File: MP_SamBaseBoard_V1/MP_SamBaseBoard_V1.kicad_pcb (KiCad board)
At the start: 4 copper layers, 80 x 60 mm, 142 parts, among them J1 MOTOR-A_CONN, J10 P1_CONN, J11 I2C_CONN, J12 I2C_CONN, J13 SAM_SWD, J14 WS2812_EXT, J15 PWR_JACK, J16 USB_B_Micro, J17 BATT_CONN, J2 MOTOR-B_CONN, J3 Adafruit_Feather_CONN, J4 DM3D-SF, J5 Conn_01x02, J6 Conn_01x02, J7 SERVO_CONN, J8 P3_CONN, J9 P2_CONN, Q1 DMP3098L, SW1 RESET, SW2 3v3_PWR_SW, SW3 SW1, SW4 SW2, U1 ESP32-WROOM-32, U10 MPU-6050, U11 IRFHM9331PbF, U12 BD5291FVE-GTR, U13 SST25VF016B-50-4C-S2AF, U2 ATSAMD51J19A-A, U3 74LVC1G125, U4 TPS62135, U5 TPS62086, U6 MAX98357AETE, U7 DRV8833RTY, U8 HDC1080, U9 MCP73871-1CC, Y1 Crystal

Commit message: update
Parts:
- removed C32, C33: 4.7uF, Capacitor_SMD:C_0603_1608Metric
- removed C44: 0.1uF, Capacitor_SMD:C_0603_1608Metric
- removed D3: LED, LED_SMD:LED_0603_1608Metric
- removed D8: PWR_LED, LED_SMD:LED_0603_1608Metric
- removed G***: LOGO, GiraffeTech-Utility:MakerPlayground_BaseBoard_logo
- removed G***: LOGO, GiraffeTech-Utility:MakerPlayground_logo_4x4mm
- removed J6: Conn_01x02, GiraffeTech-Connector:DINKLE_EK500V-2P
- removed L2: 0.47uH, GiraffeTech-Inductor:L_0806_2016Metric
- removed R23, R26, R27, R28: 10K, Resistor_SMD:R_0603_1608Metric
- removed R29: 820K, Resistor_SMD:R_0603_1608Metric
- removed R39: 1K, Resistor_SMD:R_0603_1608Metric
- removed the REF** at (185.1, 130.1)
- removed U12: BD5291FVE-GTR, Package_TO_SOT_SMD:SOT-353_SC-70-5
- added H1: 3.5mm, MountingHole:MountingHole_3.5mm, F.Cu at (218.8, 93.5)
- added H2: 3.5mm, MountingHole:MountingHole_3.5mm, F.Cu at (218.8, 102.1)
- added H3: 3.5mm, MountingHole:MountingHole_3.5mm, F.Cu at (227.3, 93.5)
- added H4: 3.5mm, MountingHole:MountingHole_3.5mm, F.Cu at (227.3, 102.1)
- added Q2: ALS-PT19-315C/L177/TR8, Diode_SMD:D_0603_1608Metric, F.Cu at (233.6, 90.5)
- C14: value 10uF -> 0.1uF; footprint Capacitor_Tantalum_SMD:CP_EIA-3216-12_Kemet-S -> Capacitor_SMD:C_0603_1608Metric
- C21: value 0.1uF -> 4.7uF
- C23: value 10uF 16V -> 10uF
- C26: value 10uF -> 4.7uF; footprint Capacitor_Tantalum_SMD:CP_EIA-3216-12_Kemet-S -> Capacitor_SMD:C_0603_1608Metric
- C28, C29: value 0.1uF -> 10uF; footprint Capacitor_SMD:C_0603_1608Metric -> Capacitor_Tantalum_SMD:CP_EIA-3216-12_Kemet-S
- C30: value 2.2nF -> 0.1uF
- C31: value 1uF -> 0.1uF
- J1: value MOTOR-A_CONN -> MA_CONN; footprint GiraffeTech-Connector:DINKLE_EK500V-2P -> GiraffeTech-Connector:TerminalBlock_DEGSON_DG300-5-2pol
- J2: value MOTOR-B_CONN -> MB_CONN; footprint GiraffeTech-Connector:DINKLE_EK500V-2P -> GiraffeTech-Connector:TerminalBlock_DEGSON_DG300-5-2pol
- J4: value DM3D-SF -> LOAD_CONN; footprint Connector_Card:microSD_HC_Hirose_DM3D-SF -> GiraffeTech-Connector:TerminalBlock_DEGSON_DG300-5-3pol
- J5: value Conn_01x02 -> SPEAKER
- L3: footprint GiraffeTech-Inductor:L_1616_2020Metric -> GiraffeTech-Inductor:SPM6530T
- R11: value 10K -> 780
- R13, R17: value 10K -> 1K
- R14: value 10K -> 20K
- R16, R18, R20: value 1K -> 10K
- R19: value 2K -> 1K
- R2: value 1M -> 10K
- SW1, SW3, SW4: footprint Button_Switch_SMD:SW_SPST_B3S-1000 -> GiraffeTech-Electromechanical:SW_Push_TS-1145A-B-A
- SW2: footprint GiraffeTech-Electromechanical:SW_SPDT_CK-JS102011JCQN -> GiraffeTech-Alps:SSSS811101
- U10: value MPU-6050 -> KXTJ3-1057; footprint Sensor_Motion:InvenSense_QFN-24_4x4mm_P0.5mm -> Package_LGA:LGA-12_2x2mm_P0.5mm
- U5: value TPS62086 -> PAM8301; footprint GiraffeTech-Texas:Texas_VSON7 -> Package_TO_SOT_SMD:SOT-23-6
- U6: value MAX98357AETE -> BQ24075; footprint Package_DFN_QFN:TQFN-16-1EP_3x3mm_P0.5mm_EP1.23x1.23mm -> Package_DFN_QFN:VQFN-16-1EP_3x3mm_P0.5mm_EP1.6x1.6mm_ThermalVias
- U8: value HDC1080 -> Sensirion_SHT3x; footprint Package_SON:Texas_PWSON-N6 -> GiraffeTech-Sensiroin:Sensirion_SHT3x
- U9: value MCP73871-1CC -> LD39200PU33R; footprint Package_DFN_QFN:QFN-20-1EP_4x4mm_P0.5mm_EP2.5x2.5mm -> Package_DFN_QFN:DFN-6-1EP_3x3mm_P0.95mm_EP1.7x2.6mm
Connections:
- net Adf_D2 renamed ESP_RESET-D2
- net Adf_D3 renamed ESP_IO0-D3
- C14 pad 1: CHG_OUT -> Net-(C14-Pad1)
- C14 pad 2: GND -> Adf_A0_DAC0
- C17 pad 1: +3V3 -> +5V
- C18 pad 1: +5V -> VIN
- C21 pad 1: +3V3 -> CHG_OUT
- C23 pad 1: VIN -> CHG_OUT
- C28 pad 1: Net-(C28-Pad1) -> +3V3
- C29 pad 1: +3V3 -> +5V
- C30 pad 1: Net-(C30-Pad1) -> +3V3
- D1 pad 1: ~PG -> GND
- D2 pad 1: STAT1 -> GND
- J10 pad 3: Adf_A1_DAC1 -> D0_RxD0
- J10 pad 4: Adf_A0_DAC0 -> Adf_A1_DAC1
- J4 pad 1: Net-(J4-Pad1) -> VIN
- J4 pad 2: Adf_D13 -> Net-(J4-Pad2)
- J4 pad 3: SPI_MISO -> GND
- J8 pad 3: Adf_D4 -> Net-(J8-Pad3)
- J8 pad 4: Adf_A4 -> Adf_A3
- J9 pad 3: Adf_A3 -> D1_TxD0
- MK1 pad 1: Net-(C32-Pad2) -> Adf_A5
- R1 pad 2: Adf_D8 -> ESP_CS
- R11 pad 1: 3v3_EN -> ILIM
- R12 pad 1: +5V -> 3v3_EN
- R12 pad 2: CE -> GND
- R13 pad 1: +5V -> ISET
- R13 pad 2: ~TE -> GND
- R14 pad 1: +5V -> TMR
- R14 pad 2: PROG2 -> GND
- R15 pad 1: +5V -> TS
- R15 pad 2: REG_SEL -> GND
- R16 pad 1: +5V -> GND
- R16 pad 2: Net-(D1-Pad2) -> EN1
- R17 pad 1: PROG3 -> ~PGOOD
- R17 pad 2: GND -> Net-(D1-Pad2)
- R18 pad 1: +5V -> CHG_OUT
- R18 pad 2: Net-(D2-Pad2) -> EN2
- R19 pad 1: PROG1 -> ~CHG
- R19 pad 2: GND -> Net-(D2-Pad2)
- R2 pad 1: +3V3 -> Net-(R2-Pad1)
- R2 pad 2: Net-(R2-Pad2) -> +3V3
- R20 pad 1: +5V -> Adf_A4
- R20 pad 2: Net-(D3-Pad2) -> GND
- R21 pad 1: THERMAL -> +3V3
- R21 pad 2: GND -> I2C_SCL
- R22 pad 2: Net-(R22-Pad2) -> I2C_SDA
- SW3 pad 1: Adf_A1_DAC1 -> D0_RxD0
- SW4 pad 1: Adf_A3 -> D1_TxD0
- U1 pad 29: Adf_D8 -> ESP_CS-D8
- U1 pad 34: D0_RxD0 -> D1_TxD0
- U1 pad 35: D1_TxD0 -> D0_RxD0
- U1 pad 9: D0_RxD0 -> ESP_BUSY-D13
- U10 pad 10: Net-(C28-Pad1) -> +3V3
- U10 pad 11: GND -> +3V3
- U10 pad 12: Net-(U10-Pad12) -> I2C_SCL
- U10 pad 2: (no net) -> I2C_SDA
- U10 pad 3: (no net) -> +3V3
- U10 pad 4: (no net) -> GND
- U10 pad 5: (no net) -> Net-(U10-Pad5)
- U10 pad 6: Net-(U10-Pad6) -> GND
- U10 pad 7: Net-(U10-Pad7) -> +3V3
- U10 pad 8: +3V3 -> GND
- U10 pad 9: Net-(R22-Pad2) -> GND
- U11 pad 1: Net-(J6-Pad2) -> Net-(J4-Pad2)
- U11 pad 2: Net-(J6-Pad2) -> Net-(J4-Pad2)
- U11 pad 3: Net-(J6-Pad2) -> Net-(J4-Pad2)
- U2 pad 35: Adf_D13 -> ESP_BUSY-D13
- U2 pad 42: Adf_D8 -> ESP_CS-D8
- U5 pad 1: 3v3_EN -> Net-(J5-Pad2)
- U5 pad 2: Net-(R2-Pad2) -> GND
- U5 pad 3: +3V3 -> Net-(C14-Pad1)
- U5 pad 4: +3V3 -> Net-(R2-Pad1)
- U5 pad 5: GND -> +3V3
- U5 pad 6: Net-(L2-Pad1) -> Net-(J5-Pad1)
- U6 pad 1: Adf_D11 -> TS
- U6 pad 10: Net-(J5-Pad2) -> CHG_OUT
- U6 pad 11: GND -> CHG_OUT
- U6 pad 12: Net-(U6-Pad12) -> ILIM
- U6 pad 13: Net-(U6-Pad13) -> +5V
- U6 pad 14: Adf_D10 -> TMR
- U6 pad 16: D1_TxD0 -> ISET
- U6 pad 2: GND -> +BATT
- U6 pad 3: GND -> +BATT
- U6 pad 4: Net-(R23-Pad2) -> GND
- U6 pad 5: Net-(U6-Pad5) -> EN2
- U6 pad 6: Net-(U6-Pad6) -> EN1
- U6 pad 7: +3V3 -> ~PGOOD
- U6 pad 8: +3V3 -> GND
- U6 pad 9: Net-(J5-Pad1) -> ~CHG
- U8 pad 4: Net-(U8-Pad4) -> I2C_SCL
- U8 pad 6: I2C_SCL -> Net-(U8-Pad6)
- U8 pad 7: Net-(U8-Pad7) -> GND
- U9 pad 1: CHG_OUT -> +3V3
- U9 pad 2: +5V -> +3V3
- U9 pad 3: REG_SEL -> GND
- U9 pad 4: PROG2 -> Net-(U9-Pad4)
- U9 pad 5: THERMAL -> 3v3_EN
- U9 pad 6: ~PG -> CHG_OUT
- U9 pad 7: STAT2 -> GND
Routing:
- net ESP_BUSY-D13: track 0.00 -> 35.8 mm, vias 0 -> 2
- net Adf_D13: track 35.8 -> 0.00 mm, vias 2 -> 0
- net GND: track 87.2 -> 119.9 mm, vias 180 -> 176
- net ~CHG: track 0.00 -> 20.1 mm, vias 0 -> 2
- net PROG1: track 20.1 -> 0.00 mm, vias 2 -> 0
- net ~TE: track 13.6 -> 0.00 mm, vias 2 -> 0
- net ~PGOOD: track 0.00 -> 12.5 mm, vias 0 -> 2
- net PROG3: track 12.5 -> 0.00 mm, vias 2 -> 0
- net Net-(J6-Pad2): track 10.00 -> 0.00 mm
- net Net-(J4-Pad2): track 0.00 -> 10.00 mm
- net STAT1: track 7.61 -> 0.00 mm
- net +3V3: track 463.7 -> 469.6 mm
- net ~PG: track 4.05 -> 0.00 mm
- net Net-(R23-Pad2): track 2.93 -> 0.00 mm
- net THERMAL: track 2.06 -> 0.00 mm
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
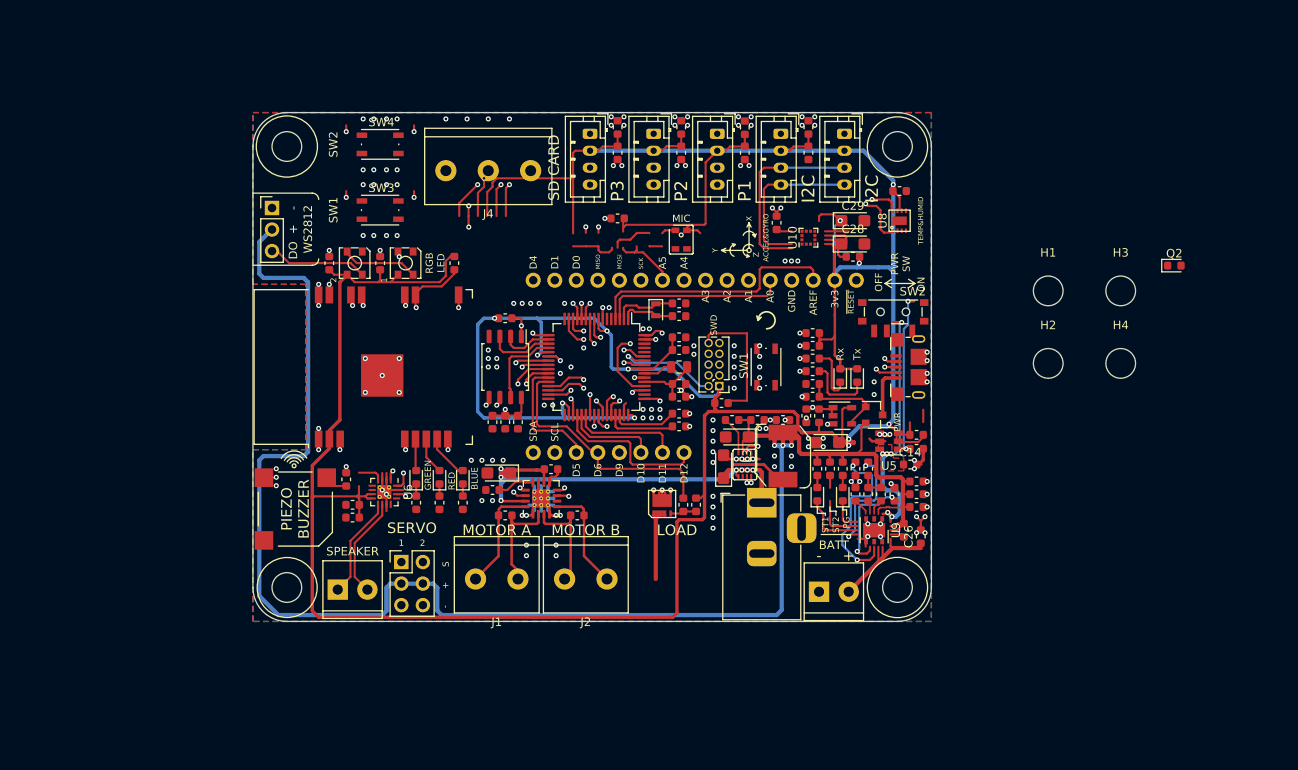
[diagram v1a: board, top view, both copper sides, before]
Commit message: Add missing components, edit foorprint
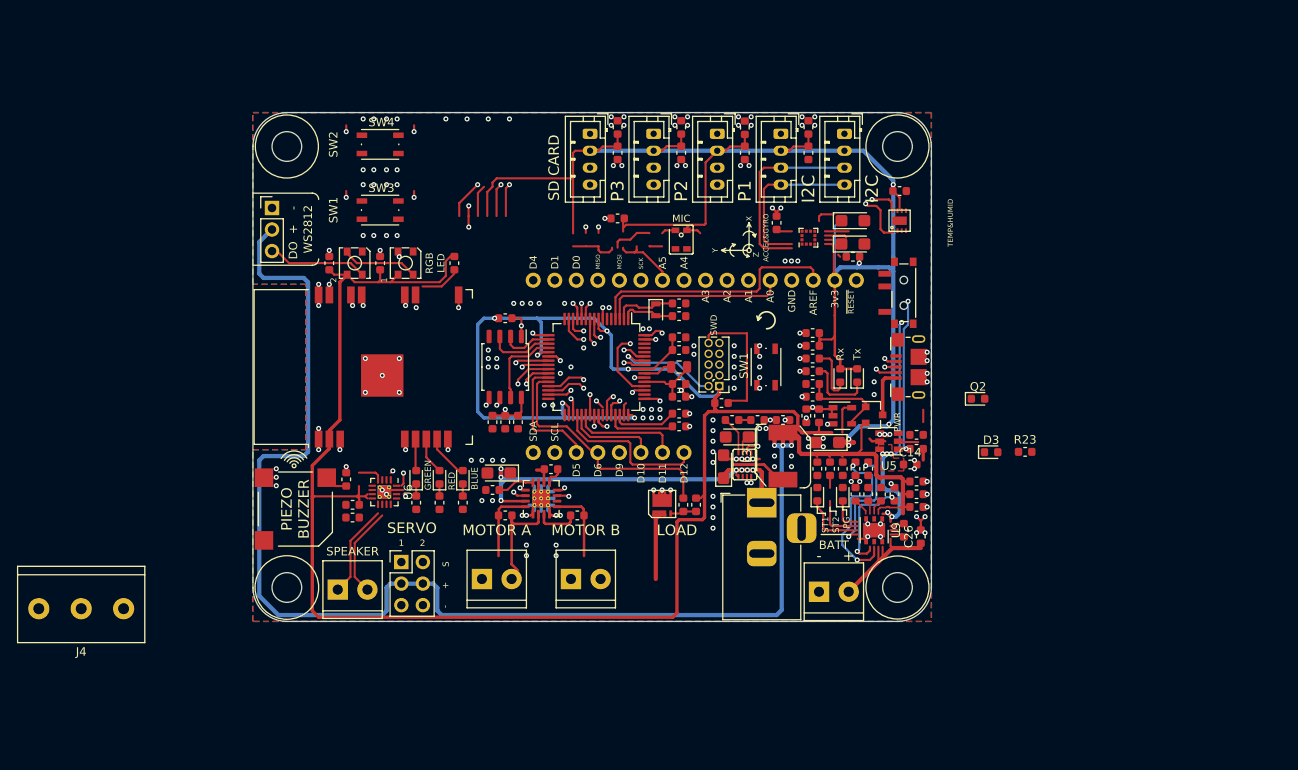
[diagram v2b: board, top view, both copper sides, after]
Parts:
- removed REF** (x4): MountingHole_3.5mm, MountingHole:MountingHole_3.5mm
- added D3: PWR_LED, LED_SMD:LED_0603_1608Metric, F.Cu at (212.0, 112.5)
- added R23: 1K, Resistor_SMD:R_0603_1608Metric, F.Cu at (216.1, 112.5)
- J1, J2: footprint GiraffeTech-Connector:TerminalBlock_DEGSON_DG300-5-2pol -> GiraffeTech-Connector:TerminalBlock_Dinkle_ED350V_1x02_P3.50mm_Horizontal
- R24: value RG -> 1K
- moved H3 99.8 mm to (129.0, 76.5), turned to 90 degrees
- moved H1 96.3 mm to (129.0, 128.5), turned to 90 degrees
- moved J4 70.5 mm to (104.8, 131.0)
- moved H4 36.7 mm to (201.0, 76.5), turned to 90 degrees
- moved H2 31.8 mm to (201.0, 128.5), turned to 90 degrees
- moved Q2 28.0 mm to (210.5, 106.2)
- moved SW2 2.57 mm to (201.8, 93.8), turned to 90 degrees
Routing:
- net Adf_D4: track 88.5 -> 72.8 mm
- net +5V: track 205.3 -> 189.8 mm
- net GND: track 119.9 -> 106.5 mm
- net +3V3: track 469.6 -> 456.3 mm, vias 13 -> 12
- net Net-(C25-Pad2): track 12.9 -> 5.06 mm
- net SPI_SCK: track 93.5 -> 87.8 mm, vias 3 -> 2
- net VIN: track 79.8 -> 74.5 mm
- net SPI_MOSI: track 77.7 -> 73.5 mm
- net Adf_D8: track 47.0 -> 42.9 mm
- net Net-(C25-Pad1): track 12.6 -> 8.80 mm
- net Net-(C24-Pad2): track 12.6 -> 8.79 mm
- net Net-(R22-Pad2): track 4.22 -> 1.15 mm
- net Adf_A3: track 88.7 -> 86.2 mm
- net Adf_A1_DAC1: track 94.0 -> 91.5 mm
- net 3v3_EN: track 20.0 -> 17.7 mm
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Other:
- board text removed: "OFF"
- board text removed: "ON"
- board text removed: "PWR SW"

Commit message: update
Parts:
- removed R33, R34: R_USB, Resistor_SMD:R_0603_1608Metric
- added C32: 0.1uF, Capacitor_SMD:C_0603_1608Metric, F.Cu at (142.0, 147.5)
- J4: footprint GiraffeTech-Connector:TerminalBlock_DEGSON_DG300-5-3pol -> GiraffeTech-Connector:TerminalBlock_Dinkle_ED350V_1x03_P3.50mm_Horizontal
- moved C21 83.2 mm to (218.5, 135.8), turned to 90 degrees
- moved C23 82.3 mm to (236.0, 108.5)
- moved J4 70.0 mm to (174.8, 128.8)
- moved R2 69.6 mm to (142.0, 143.5)
- moved U5 69.5 mm to (138.0, 142.8)
- moved C14 68.2 mm to (142.0, 145.5)
- moved C31 61.5 mm to (188.8, 86.0), turned to 270 degrees
- moved SW1 59.0 mm to (140.8, 64.0)
- moved U6 58.1 mm to (198.5, 120.0), turned to 90 degrees
- moved L3 53.3 mm to (238.5, 97.5)
- moved U4 52.3 mm to (233.0, 98.8)
- moved R6 50.9 mm to (233.0, 93.2)
- moved R8 50.2 mm to (229.8, 95.0)
- moved C18 48.4 mm to (229.0, 98.8)
- moved C28 48.3 mm to (235.8, 115.0)
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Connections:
- D3 pad 1: Net-(D3-Pad1) -> GND
- D3 pad 2: +3V3 -> Net-(D3-Pad2)
- J1 pad 1: Net-(C24-Pad1) -> Net-(C24-Pad2)
- J1 pad 2: Net-(C24-Pad2) -> Net-(C24-Pad1)
- J13 pad 7: Net-(J13-Pad7) -> (no net)
- J13 pad 8: Net-(J13-Pad8) -> (no net)
- J16 pad 2: Net-(J16-Pad2) -> USB_DM
- J16 pad 3: Net-(J16-Pad3) -> USB_DP
- J2 pad 1: Net-(C25-Pad1) -> Net-(C25-Pad2)
- J2 pad 2: Net-(C25-Pad2) -> Net-(C25-Pad1)
- J4 pad 1: VIN -> GND
- J4 pad 3: GND -> VIN
- J8 pad 3: Net-(J8-Pad3) -> (no net)
- R1 pad 2: ESP_CS -> ESP_CS-D8
- R23 pad 1: Net-(D3-Pad1) -> +3V3
- R23 pad 2: GND -> Net-(D3-Pad2)
- SW2 pad 3: Net-(SW2-Pad3) -> (no net)
- U10 pad 5: Net-(U10-Pad5) -> (no net)
- U2 pad 16: Net-(U2-Pad16) -> (no net)
- U2 pad 32: Net-(U2-Pad32) -> (no net)
- U2 pad 5: Net-(U2-Pad5) -> (no net)
- U2 pad 50: Net-(U2-Pad50) -> (no net)
- U2 pad 6: Net-(U2-Pad6) -> (no net)
- U2 pad 60: Net-(U2-Pad60) -> (no net)
- U2 pad 61: Net-(U2-Pad61) -> (no net)
- U2 pad 62: Net-(U2-Pad62) -> (no net)
- U4 pad 9: Net-(U4-Pad9) -> (no net)
- U7 pad 6: Net-(U7-Pad6) -> (no net)
- U8 pad 3: Net-(U8-Pad3) -> (no net)
- U8 pad 6: Net-(U8-Pad6) -> (no net)
- U9 pad 4: Net-(U9-Pad4) -> (no net)
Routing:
- net +3V3: track 456.3 -> 334.4 mm, vias 12 -> 7
- net GND: track 106.5 -> 30.2 mm, vias 176 -> 87
- net Adf_A3: track 86.2 -> 20.2 mm, vias 3 -> 1
- net Adf_A1_DAC1: track 91.5 -> 26.5 mm, vias 3 -> 1
- net Adf_A4: track 46.1 -> 14.9 mm
- net Net-(J16-Pad2): track 28.6 -> 0.00 mm, vias 2 -> 0
- net USB_DM: track 8.26 -> 36.9 mm, vias 0 -> 2
- net USB_DP: track 7.67 -> 35.9 mm, vias 0 -> 2
- net Net-(J16-Pad3): track 28.2 -> 0.00 mm, vias 2 -> 0
- net SPI_SCK: track 87.8 -> 60.2 mm
- net SPI_MOSI: track 73.5 -> 46.6 mm, vias 3 -> 2
- net Adf_D10: track 54.5 -> 28.7 mm, vias 2 -> 1
- net Adf_D11: track 57.1 -> 31.6 mm, vias 2 -> 1
- net +5V: track 189.8 -> 164.5 mm
- net SPI_MISO: track 81.2 -> 56.3 mm, vias 3 -> 2
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- removed copper zone on F.Cu, net CHG_OUT
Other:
- outline, holes or cut-outs redrawn
- board text added: "CHG"
- board text removed: "BATT"
- board text removed: "SD CARD"
- board text removed: "ST1"
- board text removed: "ST2"

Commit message: update
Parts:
- removed R12: 10K, Resistor_SMD:R_0603_1608Metric
- moved Q2 66.8 mm to (153.8, 75.8)
- moved R20 66.8 mm to (153.8, 77.2)
- moved R7 59.1 mm to (175.2, 107.8), turned to 180 degrees
- moved C9 58.4 mm to (187.2, 108.0), turned to 90 degrees
- moved R6 57.6 mm to (177.5, 108.5), turned to 90 degrees
- moved C12 57.2 mm to (188.8, 108.0), turned to 90 degrees
- moved C29 56.7 mm to (188.2, 119.5), turned to 270 degrees
- moved R8 56.3 mm to (175.2, 109.2)
- moved C15 56.0 mm to (190.2, 108.0), turned to 90 degrees
- moved L3 53.5 mm to (187.5, 113.5), turned to 0 degrees
- moved U4 53.3 mm to (181.2, 111.5), turned to 270 degrees
- moved C18 51.1 mm to (180.5, 114.8)
- moved C28 42.8 mm to (193.0, 114.5), turned to 270 degrees
- moved U9 39.4 mm to (196.2, 114.8)
- moved C23 34.6 mm to (202.5, 117.2), turned to 0 degrees
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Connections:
- SW2 pad 1: 3v3_EN -> GND
- SW2 pad 2: CHG_OUT -> 3v3_EN
- SW2 pad 3: (no net) -> CHG_OUT
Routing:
- net +3V3: track 334.4 -> 274.9 mm
- net VIN: track 92.5 -> 130.8 mm, vias 7 -> 3
- net +5V: track 164.5 -> 202.6 mm, vias 3 -> 5
- net CHG_OUT: track 15.1 -> 50.6 mm, vias 1 -> 3
- net ~RESET: track 69.7 -> 54.0 mm
- net ~CHG: track 0.00 -> 13.7 mm, vias 0 -> 2
- net GND: track 30.2 -> 43.4 mm, vias 87 -> 124
- net 3v3_EN: track 17.4 -> 29.2 mm, vias 1 -> 2
- net +BATT: track 0.00 -> 11.8 mm
- net SAM_TxLED: track 37.3 -> 26.8 mm, vias 2 -> 1
- net SAM_RxLED: track 30.7 -> 20.9 mm, vias 2 -> 1
- net ~PGOOD: track 0.00 -> 8.84 mm, vias 0 -> 2
- net Net-(L3-Pad1): track 0.00 -> 8.55 mm
- net Net-(D4-Pad1): track 8.24 -> 0.00 mm
- net ILIM: track 0.00 -> 8.09 mm, vias 0 -> 2
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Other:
- board text added: "7-15 VDC"
- board text added: "LOAD SWITCH"
- board text added: "Li-PO"
- board text added: "SW"

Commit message: update
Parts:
- removed R25: 10K, Resistor_SMD:R_0603_1608Metric
- added F1: 6V Trip 4A, Fuse:Fuse_1206_3216Metric, F.Cu at (197.5, 102.5)
- added F2: 16V Trip 4A, Fuse:Fuse_1812_4532Metric, F.Cu at (173.5, 118.8)
- added F3: 6V Trip 2.5A, Fuse:Fuse_1812_4532Metric, F.Cu at (136.5, 89.0)
- added Q3: BSS138-7-F, Package_TO_SOT_SMD:SOT-23, F.Cu at (186.5, 99.0)
- added R12: 10K, Resistor_SMD:R_0603_1608Metric, F.Cu at (188.5, 108.0)
- added U12: IRFHM9331PbF, GiraffeTech-IR:PQFN_3x3mm_IRFHM9331TRPbF, F.Cu at (191.0, 108.0)
- added U14: IRFHM9331PbF, GiraffeTech-IR:PQFN_3x3mm_IRFHM9331TRPbF, F.Cu at (181.2, 114.2)
- R24: value 1K -> 10K
- U11: value IRFHM9331PbF -> IRFHM3911PbF; footprint GiraffeTech-IR:PQFN_3x3mm -> GiraffeTech-IR:PQFN_3x3mm_IRFHM3911PbF
- moved SW1 65.3 mm to (201.8, 87.2), turned to 180 degrees
- moved C9 39.9 mm to (226.2, 99.5), turned to 180 degrees
- moved C12 38.8 mm to (226.2, 98.0), turned to 180 degrees
- moved C15 37.8 mm to (226.2, 96.5), turned to 180 degrees
- moved R10 16.6 mm to (191.5, 88.8), turned to 0 degrees
- moved R4 12.8 mm to (184.5, 104.2), turned to 180 degrees
- moved R3 11.3 mm to (184.5, 105.8), turned to 0 degrees
- moved C43 11.0 mm to (140.8, 79.2), turned to 0 degrees
- moved R8 9.46 mm to (184.5, 107.2)
- moved C42 8.11 mm to (140.8, 85.8), turned to 0 degrees
- moved R35 7.04 mm to (199.0, 108.0)
- moved Q1 6.04 mm to (194.5, 102.5), turned to 90 degrees
- moved R5 4.60 mm to (197.5, 108.0)
- moved R21 4.51 mm to (191.5, 87.2)
- moved R22 4.51 mm to (191.5, 85.8)
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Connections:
- J14 pad 2: +5V -> Net-(F3-Pad2)
- J15 pad 1: VIN -> VIN_RAW
- J16 pad 1: VBUS -> Net-(F1-Pad2)
- J4 pad 3: VIN -> Net-(F2-Pad2)
- R24 pad 1: Net-(R24-Pad1) -> GND
- R8 pad 1: +5V -> VIN
- U11 pad 1: Net-(J4-Pad2) -> GND
- U11 pad 2: Net-(J4-Pad2) -> GND
- U11 pad 3: Net-(J4-Pad2) -> GND
- U11 pad 4: Net-(R24-Pad1) -> Adf_D6
- U11 pad 5: GND -> Net-(J4-Pad2)
- U11 pad 6: GND -> Net-(J4-Pad2)
- U11 pad 7: GND -> Net-(J4-Pad2)
- U11 pad 8: GND -> Net-(J4-Pad2)
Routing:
- net VIN: track 130.8 -> 62.5 mm, vias 3 -> 2
- net USB_PWR_SEL: track 36.2 -> 20.3 mm, vias 2 -> 1
- net +3V3: track 274.9 -> 259.4 mm
- net VIN_RAW: track 0.00 -> 13.4 mm
- net +5V: track 202.6 -> 189.5 mm
- net Net-(J4-Pad2): track 10.3 -> 18.8 mm
- net Net-(F2-Pad2): track 0.00 -> 7.86 mm
- net PG_5V: track 7.78 -> 0.00 mm
- net USB_ID: track 17.3 -> 10.0 mm, vias 0 -> 1
- net VBUS: track 6.61 -> 0.00 mm
- net Net-(Q1-Pad1): track 5.70 -> 0.00 mm
- net GND: track 43.4 -> 40.0 mm
- net Net-(R24-Pad1): track 3.10 -> 0.00 mm
- net Net-(R6-Pad2): track 7.10 -> 10.1 mm, vias 0 -> 2
- net Adf_D6: track 26.2 -> 23.7 mm
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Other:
- board text added: "OFF"
- board text added: "ON"
- board text removed: "SWD"

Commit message: update
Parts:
- moved C12 37.5 mm to (192.8, 114.8)
- moved C15 37.5 mm to (192.8, 113.2)
- moved C9 37.5 mm to (192.8, 116.2)
- moved C30 28.5 mm to (214.5, 94.5), turned to 0 degrees
- moved U10 27.5 mm to (214.5, 96.5)
- moved C14 27.1 mm to (139.8, 118.5)
- moved C32 27.1 mm to (139.8, 120.5)
- moved R2 27.1 mm to (139.8, 116.5)
- moved C31 26.7 mm to (214.5, 93.0), turned to 0 degrees
- moved U5 22.4 mm to (135.5, 120.5)
- moved C19 22.3 mm to (156.0, 82.8)
- moved MK1 22.3 mm to (153.8, 82.7)
- moved D4 20.9 mm to (195.8, 100.5), turned to 0 degrees
- moved U3 19.5 mm to (175.2, 109.0), turned to 0 degrees
- moved R30 19.1 mm to (192.8, 100.5)
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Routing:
- net +3V3: track 259.4 -> 381.1 mm, vias 7 -> 17
- net D1_TxD0: track 88.2 -> 47.2 mm
- net ESP_CS-D8: track 0.00 -> 40.9 mm, vias 0 -> 2
- net Adf_D8: track 38.5 -> 0.00 mm, vias 2 -> 0
- net D0_RxD0: track 83.2 -> 48.6 mm, vias 3 -> 2
- net USB_ID: track 10.0 -> 44.0 mm, vias 1 -> 3
- net Adf_A0_DAC0: track 21.9 -> 50.6 mm, vias 0 -> 1
- net Net-(Q3-Pad3): track 1.46 -> 29.8 mm, vias 0 -> 3
- net USB_PWR_SEL: track 20.3 -> 45.2 mm, vias 1 -> 2
- net VIN: track 62.5 -> 87.3 mm, vias 2 -> 7
- net Net-(Q1-Pad1): track 0.00 -> 23.5 mm, vias 0 -> 2
- net I2C_SDA: track 83.8 -> 104.3 mm
- net ESP_BUSY-D13: track 17.5 -> 2.02 mm
- net ~RESET: track 54.0 -> 69.0 mm
- net I2C_SCL: track 83.0 -> 97.1 mm
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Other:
- board text added: "4A LOAD SWITCH"
- board text added: "ACCEL"
- board text added: "~RST"
- board text removed: "ACCEL&GYRO"
- board text removed: "LOAD SWITCH"
- board text removed: "OFF"

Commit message: update
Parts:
- moved Q2 12.8 mm to (154.2, 88.5)
- moved R20 12.8 mm to (154.2, 90.0)
- moved MK1 8.31 mm to (149.7, 90.0), turned to 90 degrees
- moved C19 8.00 mm to (149.8, 87.8), turned to 0 degrees
- moved R1 5.40 mm to (143.5, 91.5), turned to 0 degrees
- moved J14 5.01 mm to (127.0, 88.8), turned to 180 degrees
- moved C42 4.26 mm to (143.5, 82.5), turned to 270 degrees
- moved C43 4.07 mm to (143.5, 76.2), turned to 270 degrees
- moved C32 3.95 mm to (136.0, 121.8), turned to 270 degrees
- moved U5 3.72 mm to (139.0, 121.8)
- moved R32 2.50 mm to (136.0, 118.2), turned to 270 degrees
- moved R2 2.47 mm to (138.0, 118.2), turned to 90 degrees
- moved F3 0.50 mm to (136.5, 88.5), turned to 0 degrees
- moved C14 0.35 mm to (140.0, 118.2), turned to 90 degrees
- moved D6 0.25 mm to (140.8, 82.5), turned to 270 degrees
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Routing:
- net +3V3: track 381.1 -> 424.5 mm
- net ESP_BUSY-D13: track 2.02 -> 31.1 mm, vias 1 -> 2
- net WS2812_EXT: track 0.00 -> 22.9 mm, vias 0 -> 1
- net D1_TxD0: track 47.2 -> 69.0 mm, vias 2 -> 3
- net D0_RxD0: track 48.6 -> 66.4 mm, vias 2 -> 3
- net Adf_A0_DAC0: track 50.6 -> 67.9 mm, vias 1 -> 2
- net Net-(F3-Pad2): track 0.00 -> 13.7 mm
- net WS2812_INT: track 57.9 -> 66.2 mm, vias 1 -> 2
- net Net-(J5-Pad1): track 0.00 -> 7.88 mm
- net Net-(J5-Pad2): track 0.00 -> 6.69 mm
- net GND: track 51.6 -> 58.2 mm, vias 167 -> 178
- net Adf_D5: track 46.7 -> 51.7 mm
- net Net-(D6-Pad2): track 0.00 -> 4.93 mm
- net Adf_D7: track 37.0 -> 41.6 mm
- net Adf_D4: track 52.2 -> 56.5 mm
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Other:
- outline, holes or cut-outs redrawn
